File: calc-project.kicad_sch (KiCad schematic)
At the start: 54 parts, among them J2 Conn_01x08_Socket, J3 Conn_01x08_Socket, J4 Conn_01x08_Socket, SW1 SW_Push_45deg, SW10 SW_Push_45deg, SW11 SW_Push_45deg, SW12 SW_Push_45deg, SW13 SW_Push_45deg, SW14 SW_Push_45deg, SW15 SW_Push_45deg, SW16 SW_Push_45deg, SW17 SW_Push_45deg, SW18 SW_Push_45deg, SW19 SW_Push_45deg, SW2 SW_Push_45deg, SW20 SW_Push_45deg, SW21 SW_Push_45deg, SW22 SW_Push_45deg, SW23 SW_Push_45deg, SW24 SW_Push_45deg, SW25 SW_Push_45deg, SW26 SW_Push_45deg, SW27 SW_Push_45deg, SW28 SW_Push_45deg, SW29 SW_Push_45deg, SW3 SW_Push_45deg, SW30 SW_Push_45deg, SW31 SW_Push_45deg, SW32 SW_Push_45deg, SW33 SW_Push_45deg, SW34 SW_Push_45deg, SW35 SW_Push_45deg, SW36 SW_Push_45deg, SW37 SW_Push_45deg, SW38 SW_Push_45deg, SW39 SW_Push_45deg, SW4 SW_Push_45deg, SW40 SW_Push_45deg, SW41 SW_Push_45deg, SW42 SW_Push_45deg, SW43 SW_Push_45deg, SW44 SW_Push_45deg, SW45 SW_Push_45deg, SW46 SW_Push_45deg, SW47 SW_Push_45deg, SW48 SW_Push_45deg, SW5 SW_Push_45deg, SW6 SW_Push_45deg, SW7 SW_Push_45deg, SW8 SW_Push_45deg, SW9 SW_Push_45deg

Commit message: added rpi pico, took away connectors, idk what else
idk what i did
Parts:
- removed J2, J3, J4: Conn_01x08_Socket, Connector_PinSocket_1.00mm:PinSocket_1x08_P1.00mm_Vertical, symbol Connector:Conn_01x08_Socket
- removed SW37, SW38, SW39, SW40, SW41, SW42, SW43, SW44, SW45, SW46, SW47, SW48: SW_Push_45deg, Library:SW_TL3315NF160Q, symbol Switch:SW_Push_45deg
- added J1: PinSocket_1x20_Right, Connector_PinSocket_2.54mm:PinSocket_1x20_P2.54mm_Vertical_SMD_Pin1Left, symbol Custom parts:PinSocket_1x20_Right
- added J2: PinSocket_1x20_Left, Connector_PinSocket_2.54mm:PinSocket_1x20_P2.54mm_Vertical_SMD_Pin1Left, symbol Custom parts:PinSocket_1x20_Left
- R1: value 100 -> 10
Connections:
- net +3.3V: now also LCD1.13 (RDX), J1.36 (3V3_OUT); no longer LCD1.6 (IM3)
- net GND: now also LCD1.6 (IM3), J1.23 (GND), J1.28 (GND), J1.38 (GND), J2.18 (GND), J2.3 (GND), J2.8 (GND); no longer LCD1.13 (RDX)
- net col 2: now reaches SW10.1, SW16.1, SW22.1, SW28.1, SW34.1, SW4.1
- net col 2: now also J2.4 (GP2)
- net row 0: now reaches SW1.2, SW2.2, SW3.2, SW4.2, SW5.2, SW6.2
- net row 0: now also J2.9 (GP6)
- net col 0: now reaches SW12.1, SW18.1, SW24.1, SW30.1, SW36.1, SW6.1
- net col 0: now also J2.1 (GP0)
- net col 4: now reaches SW14.1, SW2.1, SW20.1, SW26.1, SW32.1, SW8.1
- net col 4: now also J2.6 (GP4)
- net row 4: now reaches SW25.2, SW26.2, SW27.2, SW28.2, SW29.2, SW30.2
- net row 4: now also J2.13 (GND)
- net DISPLAY_DATA_IN: now reaches LCD1.33 (SDA)
- net DISPLAY_DATA_IN: now also J1.25 (GP19)
- net Write strobe sig: now reaches LCD1.12 (WRX)
- net Write strobe sig: now also J1.24 (GP18)
- net Data/Comm select: now reaches LCD1.11 (DCX)
- net Data/Comm select: now also J1.21 (GP16)
- net Chip select: now reaches LCD1.10 (~{CSX})
- net Chip select: now also J1.22 (GP17)
- net col 1: now reaches SW11.1, SW17.1, SW23.1, SW29.1, SW35.1, SW5.1
- net col 1: now also J2.2 (GP1)
- net row 1: now reaches SW10.2, SW11.2, SW12.2, SW7.2, SW8.2, SW9.2
- net row 1: now also J2.10 (GP7)
- net row 3: now reaches SW19.2, SW20.2, SW21.2, SW22.2, SW23.2, SW24.2
- net row 3: now also J2.12 (GP9)
- net col 5: now reaches SW1.1, SW13.1, SW19.1, SW25.1, SW31.1, SW7.1
- net col 5: now also J2.7 (GP5)
- net row 5: now reaches SW31.2, SW32.2, SW33.2, SW34.2, SW35.2, SW36.2
- net row 5: now also J2.14 (GP10)
- net col 3: now reaches SW15.1, SW21.1, SW27.1, SW3.1, SW33.1, SW9.1
- net col 3: now also J2.5 (GP3)
- net row 2: now reaches SW13.2, SW14.2, SW15.2, SW16.2, SW17.2, SW18.2
- net row 2: now also J2.11 (GP8)
- net RESET: now reaches LCD1.38 (~{RESX})
- net RESET: now also J1.26 (GP20)
- no-connect marks 27 -> 38
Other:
- moved on the sheet: C1, SW1, SW10, SW11, SW12, SW13, SW14, SW15, SW16, SW17, SW18, SW19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

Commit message: idek if this is progress or not
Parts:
- added C2, C4: 4.7u, Capacitor_SMD:C_0201_0603Metric_Pad0.64x0.40mm_HandSolder, symbol Device:C
- added C3, C5: 100nF, Capacitor_SMD:C_0201_0603Metric_Pad0.64x0.40mm_HandSolder, symbol Device:C
- added D1: D_Schottky, symbol Device:D_Schottky
- added L1: 22 µH, symbol Device:L
- added R2, R3: 10, Resistor_SMD:R_0201_0603Metric_Pad0.64x0.40mm_HandSolder, symbol Device:R
- added R4: 10k, Resistor_SMD:R_0201_0603Metric_Pad0.64x0.40mm_HandSolder, symbol Device:R
- added U1: TPS61165DBV, Package_TO_SOT_SMD:SOT-23-6, symbol Driver_LED:TPS61165DBV
- R1: value 10 -> 10k
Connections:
- net +3.3V: now also R1.2, R2.2; no longer R1.1
- net Chip select: now also R2.1
- net GND: now also LCD1.14 (DB0), LCD1.15 (DB1), LCD1.16 (DB2), LCD1.17 (DB3), LCD1.18 (DB4), LCD1.19 (DB5), LCD1.20 (DB6), LCD1.21 (DB7), LCD1.22 (DB8), LCD1.23 (DB9), LCD1.24 (DB10), LCD1.25 (DB11), LCD1.26 (DB12), LCD1.27 (DB13), LCD1.28 (DB14), LCD1.29 (DB15), LCD1.30 (DB16), LCD1.31 (DB17), C2.1, C3.1, C4.2, C5.1, R3.2, R4.1, U1.4 (GND); no longer LCD1.39 (LEDK)
- net RESET: now also R1.1
- net at LCD1.40 (LEDA): now also D1.1 (K); no longer R1.2
- net LED_CTRL: now reaches J1.29 (GP22)
- net LED_CTRL: now also R4.2, U1.2 (CTRL)
- net VSYS(3-5V): now reaches J1.39 (VSYS)
- net VSYS(3-5V): now also C2.2, L1.1, U1.1 (VIN)
- new net: C3.2, C5.2, U1.5 (COMP)
- new net: D1.2 (A), L1.2, U1.3 (SW)
- new net: LCD1.39 (LEDK), R3.1, U1.6 (FB)
- no-connect marks 38 -> 19
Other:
- note added: "gpt says 5ohms? check later"
- moved on the sheet: C1, LCD1

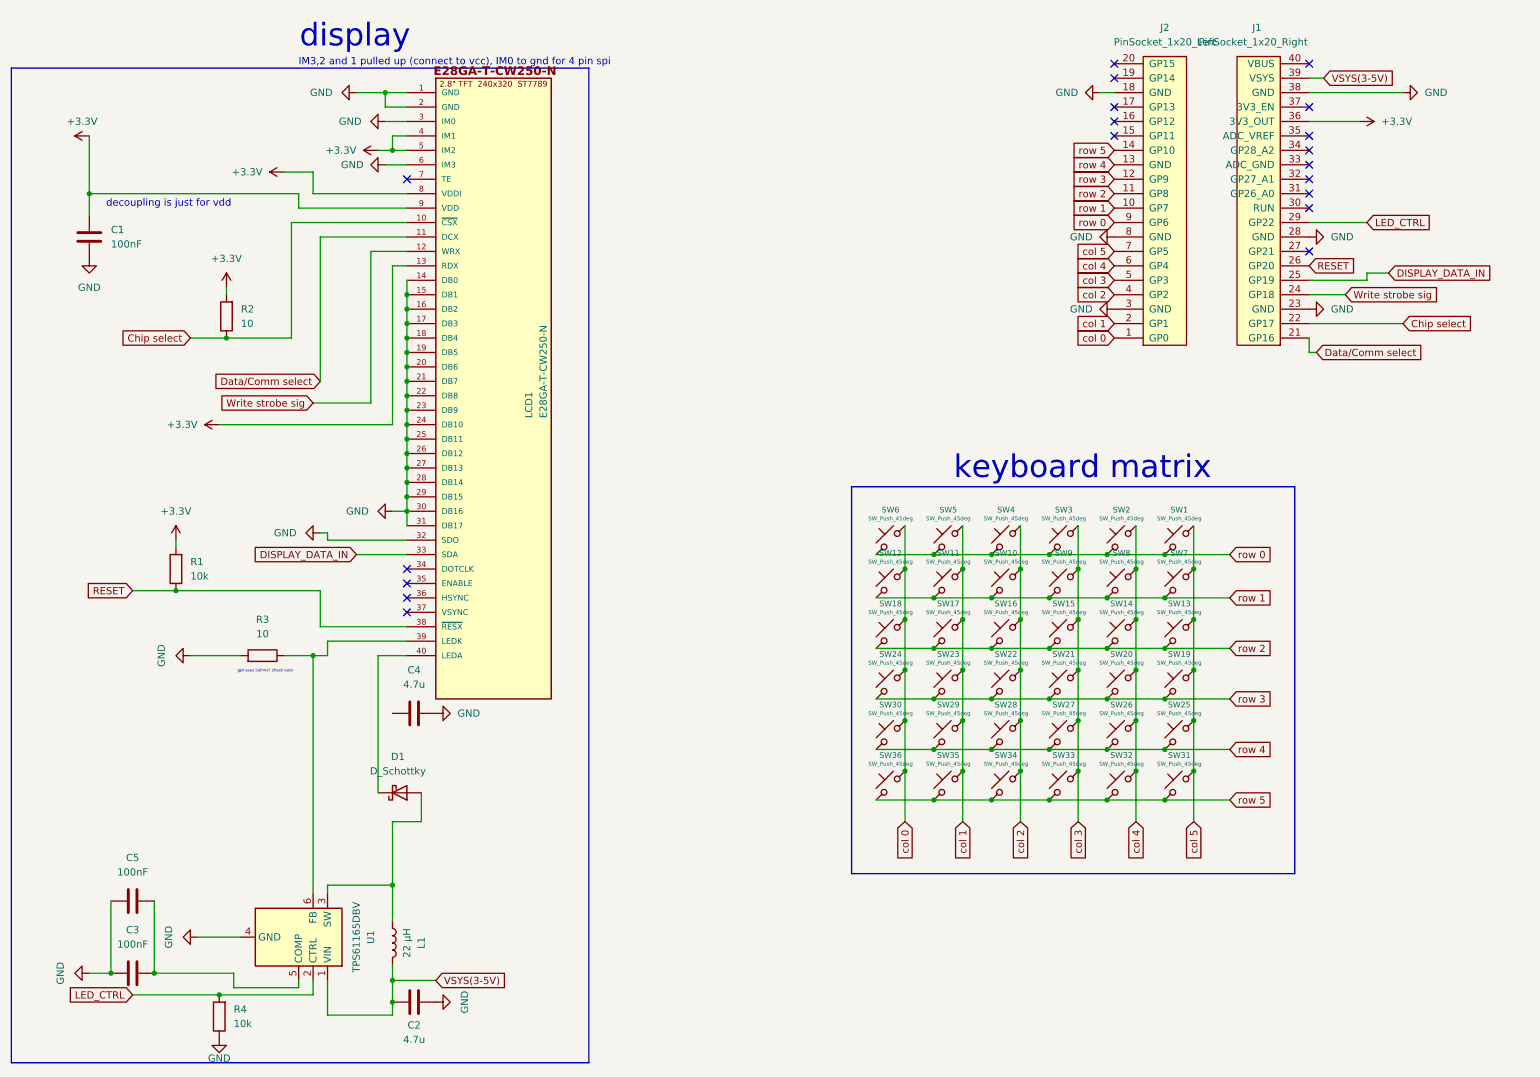
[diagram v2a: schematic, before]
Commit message: we're now setting ourselves up for new screen, still need alignment
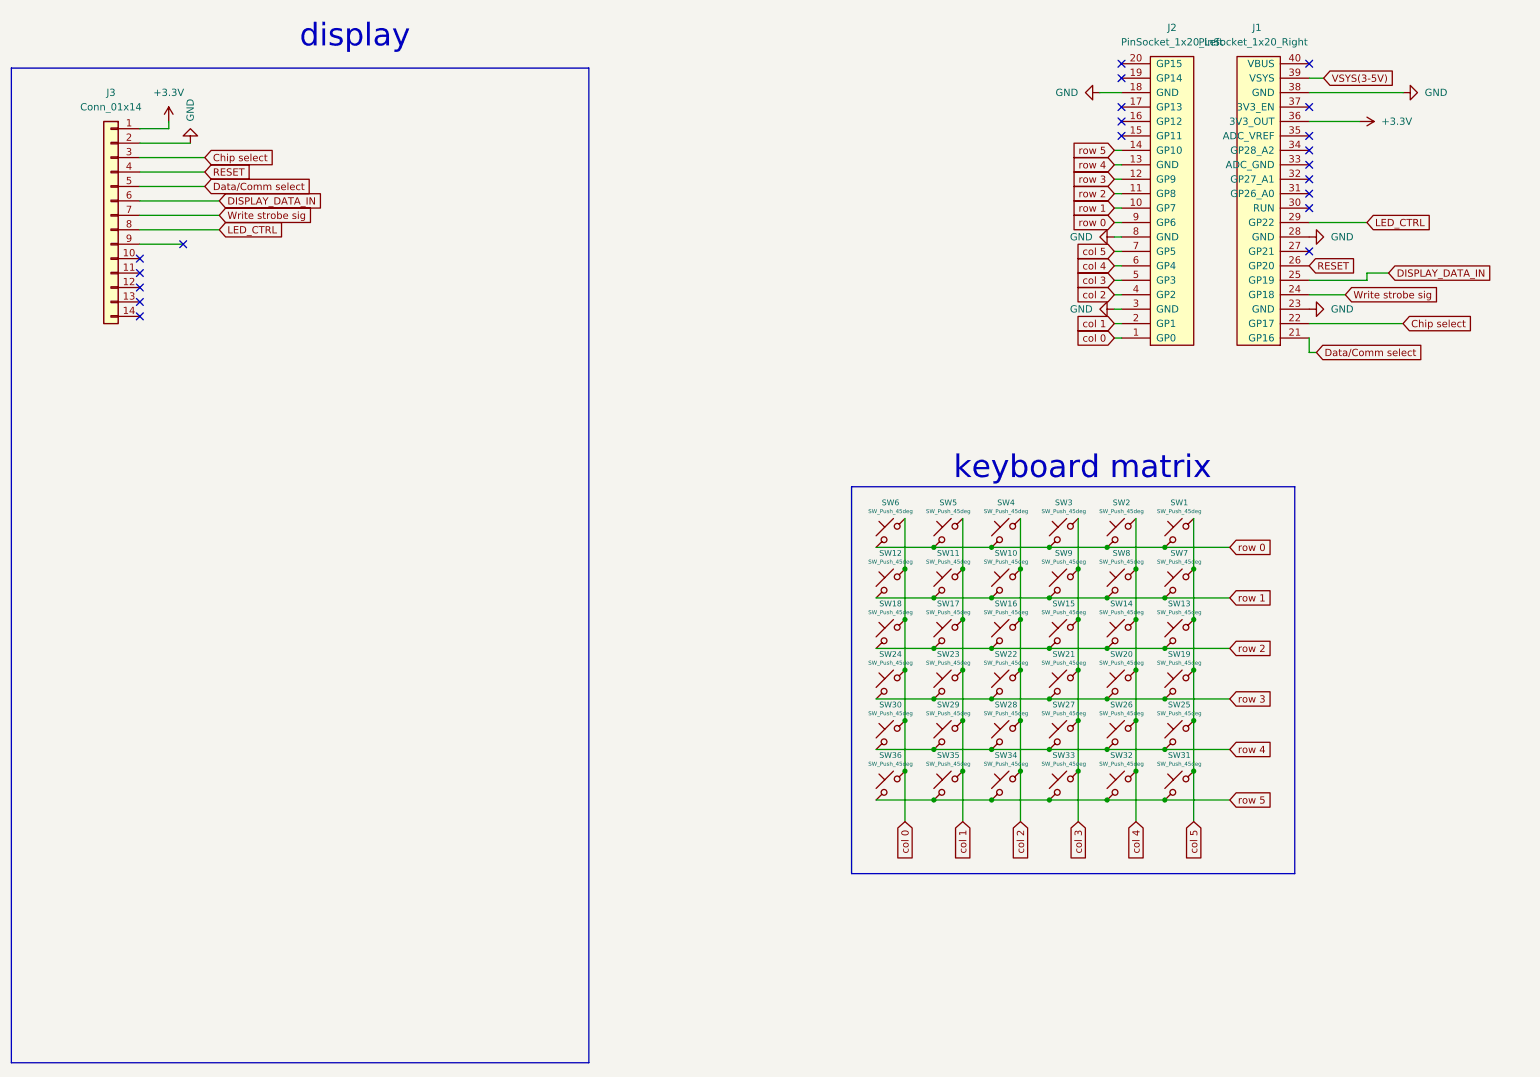
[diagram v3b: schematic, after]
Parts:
- removed C1, C3, C5: 100nF, Capacitor_SMD:C_0201_0603Metric_Pad0.64x0.40mm_HandSolder, symbol Device:C
- removed C2, C4: 4.7u, Capacitor_SMD:C_0201_0603Metric_Pad0.64x0.40mm_HandSolder, symbol Device:C
- removed D1: D_Schottky, symbol Device:D_Schottky
- removed L1: 22 µH, symbol Device:L
- removed LCD1: E28GA-T-CW250-N, Library:CONN40_FH12S-40S_HIR, symbol Custom parts:E28GA-T-CW250-N
- removed R1, R4: 10k, Resistor_SMD:R_0201_0603Metric_Pad0.64x0.40mm_HandSolder, symbol Device:R
- removed R2, R3: 10, Resistor_SMD:R_0201_0603Metric_Pad0.64x0.40mm_HandSolder, symbol Device:R
- removed U1: TPS61165DBV, Package_TO_SOT_SMD:SOT-23-6, symbol Driver_LED:TPS61165DBV
- added J3: Conn_01x14, Library:castel_toScreen, symbol Connector_Generic:Conn_01x14
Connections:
- net +3.3V: now also J3.1 (Pin_1)
- net Chip select: now also J3.3 (Pin_3)
- net DISPLAY_DATA_IN: now also J3.6 (Pin_6)
- net Data/Comm select: now also J3.5 (Pin_5)
- net GND: now also J3.2 (Pin_2)
- net LED_CTRL: now also J3.8 (Pin_8)
- net RESET: now also J3.4 (Pin_4)
- net Write strobe sig: now also J3.7 (Pin_7)
- no-connect marks 19 -> 20
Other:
- note removed: "IM3,2 and 1 pulled up (connect to vcc), IM0 to gnd for 4 pin spi"
- note removed: "decoupling is just for vdd"
- note removed: "gpt says 5ohms? check later"
- moved on the sheet: J2, SW1, SW2, SW3, SW4, SW5, SW6

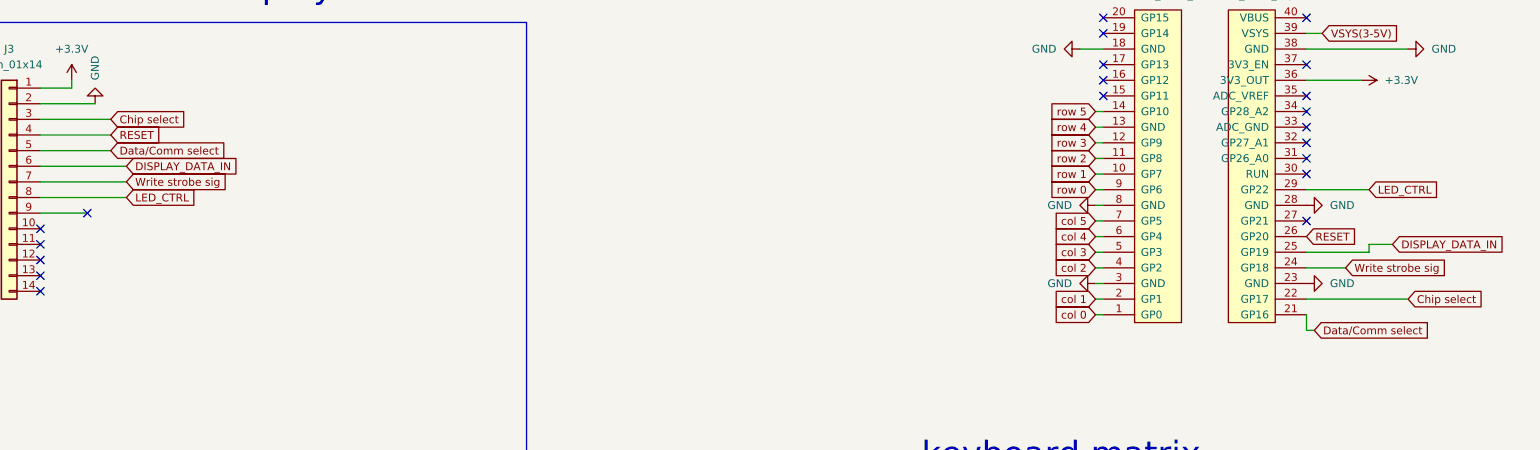
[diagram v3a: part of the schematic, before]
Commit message: fixed names, seems like schematic is good
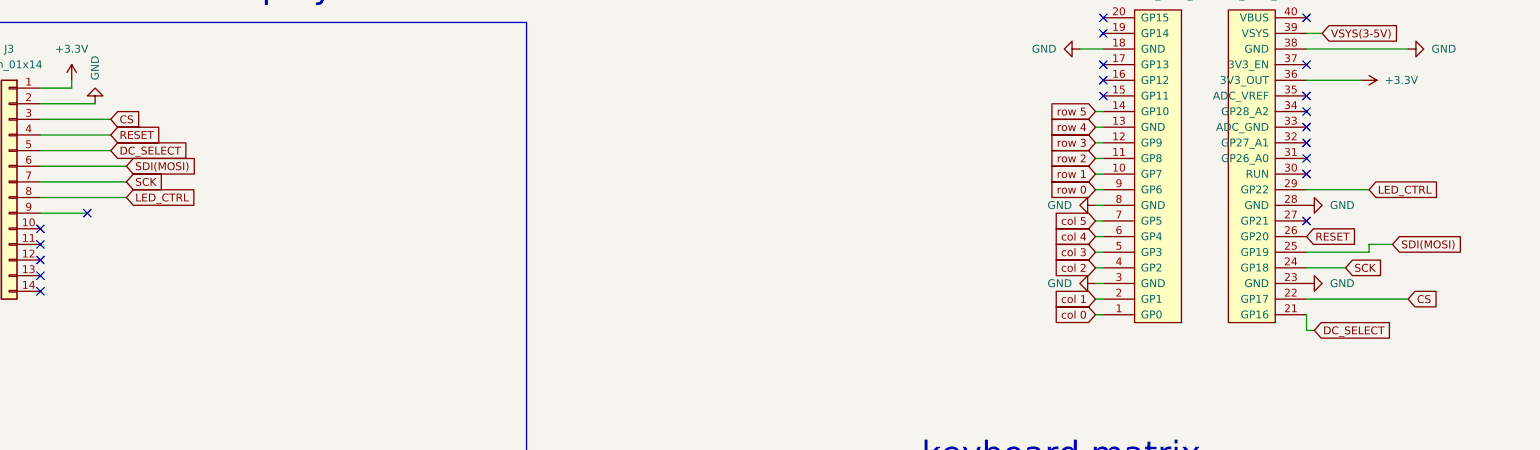
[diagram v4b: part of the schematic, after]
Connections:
- net Chip select renamed CS
- net DISPLAY_DATA_IN renamed SDI(MOSI)
- net Data/Comm select renamed DC_SELECT
- net Write strobe sig renamed SCK
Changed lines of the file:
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@@
 		)
 	)
-	(global_label "Data{slash}Comm select"
+	(global_label "DC_SELECT"
 		(shape input)
 		(at 241.3 72.39 0)
@@
 		)
 		(property "Intersheetrefs" "${INTERSHEET_REFS}"
-			(at 262.3674 72.39 0)
+			(at 254.566 72.39 0)
 			(hide yes)
 			(show_name no)
@@
 		)
 	)
-	(global_label "DISPLAY_DATA_IN"
+	(global_label "SDI(MOSI)"
 		(shape input)
 		(at 48.26 45.72 0)
@@
 		)
 		(property "Intersheetrefs" "${INTERSHEET_REFS}"
-			(at 67.0901 45.72 0)
-			(hide yes)
-			(show_name no)
-			(do_not_autoplace no)
-			(effects
-				(font
-					(size 1.27 1.27)
-				)
-				(justify left)
-			)
-		)
-	)
-	(global_label "Chip select"
+			(at 60.6191 45.72 0)
+			(hide yes)
+			(show_name no)
+			(do_not_autoplace no)
+			(effects
+				(font
+					(size 1.27 1.27)
+				)
+				(justify left)
+			)
+		)
+	)
+	(global_label "CS"
 		(shape input)
 		(at 45.72 38.1 0)
@@
 		)
 		(property "Intersheetrefs" "${INTERSHEET_REFS}"
-			(at 59.5304 38.1 0)
+			(at 51.1847 38.1 0)
 			(hide yes)
 			(show_name no)
@@
 		)
 	)
-	(global_label "Write strobe sig"
+	(global_label "SCK"
 		(shape input)
 		(at 48.26 48.26 0)
@@
 		)
 		(property "Intersheetrefs" "${INTERSHEET_REFS}"
-			(at 66.5456 48.26 0)
+			(at 54.9947 48.26 0)
 			(hide yes)
 			(show_name no)
@@
 		)
 	)
+	(global_label "CS"
+		(shape input)
+		(at 256.54 67.31 0)
+		(fields_autoplaced yes)
+		(effects
+			(font
+				(size 1.27 1.27)
+			)
+			(justify left)
+		)
+		(property "Intersheetrefs" "${INTERSHEET_REFS}"
+			(at 262.0047 67.31 0)
+			(hide yes)
+			(show_name no)
+			(do_not_autoplace no)
+			(effects
+				(font
+					(size 1.27 1.27)
+				)
+				(justify left)
+			)
+		)
+	)
 	(global_label "col 1"
 		(shape input)
@@
 		)
 	)
-	(global_label "Write strobe sig"
+	(global_label "SCK"
 		(shape input)
 		(at 246.38 62.23 0)
@@
 		)
 		(property "Intersheetrefs" "${INTERSHEET_REFS}"
-			(at 264.6656 62.23 0)
-			(hide yes)
-			(show_name no)
-			(do_not_autoplace no)
-			(effects
-				(font
-					(size 1.27 1.27)
-				)
-				(justify left)
-			)
-		)
-	)
-	(global_label "Data{slash}Comm select"
+			(at 253.1147 62.23 0)
+			(hide yes)
+			(show_name no)
+			(do_not_autoplace no)
+			(effects
+				(font
+					(size 1.27 1.27)
+				)
+				(justify left)
+			)
+		)
+	)
+	(global_label "DC_SELECT"
 		(shape input)
 		(at 45.72 43.18 0)
@@
 		)
 		(property "Intersheetrefs" "${INTERSHEET_REFS}"
-			(at 66.7874 43.18 0)
+			(at 58.986 43.18 0)
 			(hide yes)
 			(show_name no)
@@
 		)
 	)
-	(global_label "Chip select"
-		(shape input)
-		(at 256.54 67.31 0)
-		(fields_autoplaced yes)
-		(effects
-			(font
-				(size 1.27 1.27)
-			)
-			(justify left)
-		)
-		(property "Intersheetrefs" "${INTERSHEET_REFS}"
-			(at 270.3504 67.31 0)
-			(hide yes)
-			(show_name no)
-			(do_not_autoplace no)
-			(effects
-				(font
-					(size 1.27 1.27)
-				)
-				(justify left)
-			)
-		)
-	)
 	(global_label "row 4"
 		(shape input)
@@
 		)
 	)
-	(global_label "DISPLAY_DATA_IN"
+	(global_label "SDI(MOSI)"
 		(shape input)
 		(at 254 58.42 0)
@@
 		)
 		(property "Intersheetrefs" "${INTERSHEET_REFS}"
-			(at 272.8301 58.42 0)
-			(hide yes)
-			(show_name no)
+			(at 266.3591 58.42 0)
+			(hide yes)
+			(show_name no)
